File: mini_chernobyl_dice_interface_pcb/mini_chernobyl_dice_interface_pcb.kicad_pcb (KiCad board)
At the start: 2 copper layers, 148 x 49 mm, 23 parts, among them SW1 SW_Push, SW2 ROTARY-ENCODER, U1 CC56-12EWA, U2 CC56-12EWA

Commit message: finish routing
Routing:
- net Net-(H2-Pad8): track 0.00 -> 137.2 mm
- net Net-(H2-Pad7): track 0.00 -> 130.5 mm, vias 0 -> 1
- net Net-(H1-Pad7): track 0.00 -> 101.6 mm
- net Net-(H3-Pad1): track 0.00 -> 81.0 mm
- net Net-(H2-Pad5): track 0.00 -> 73.2 mm, vias 0 -> 1
- net Net-(H2-Pad4): track 0.00 -> 73.1 mm, vias 0 -> 2
- net Net-(H2-Pad3): track 0.00 -> 72.4 mm, vias 0 -> 3
- net Net-(H2-Pad2): track 0.00 -> 70.8 mm, vias 0 -> 1
- net Net-(H3-Pad3): track 0.00 -> 63.0 mm
- net Net-(H3-Pad2): track 0.00 -> 63.0 mm
- net Net-(H2-Pad1): track 0.00 -> 62.8 mm, vias 0 -> 3
- net Net-(H3-Pad4): track 0.00 -> 57.9 mm
- net Net-(H2-Pad6): track 0.00 -> 57.4 mm, vias 0 -> 2
- net Net-(H3-Pad5): track 0.00 -> 54.9 mm
- net Net-(D1-Pad1): track 0.00 -> 47.1 mm, vias 0 -> 1
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- added copper zone on F.Cu, net GND

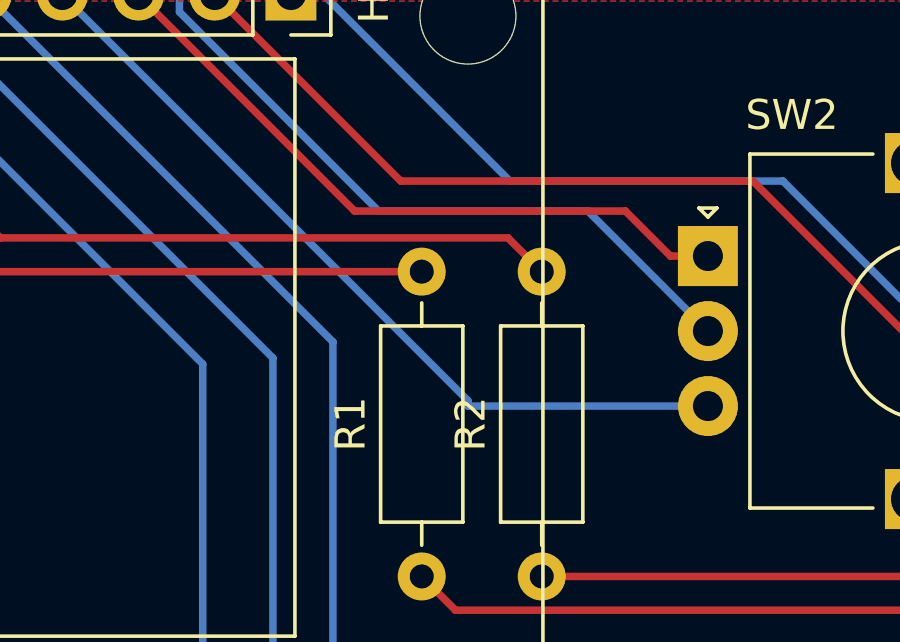
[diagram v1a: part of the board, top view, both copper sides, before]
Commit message: add and clean up labels on pcbs
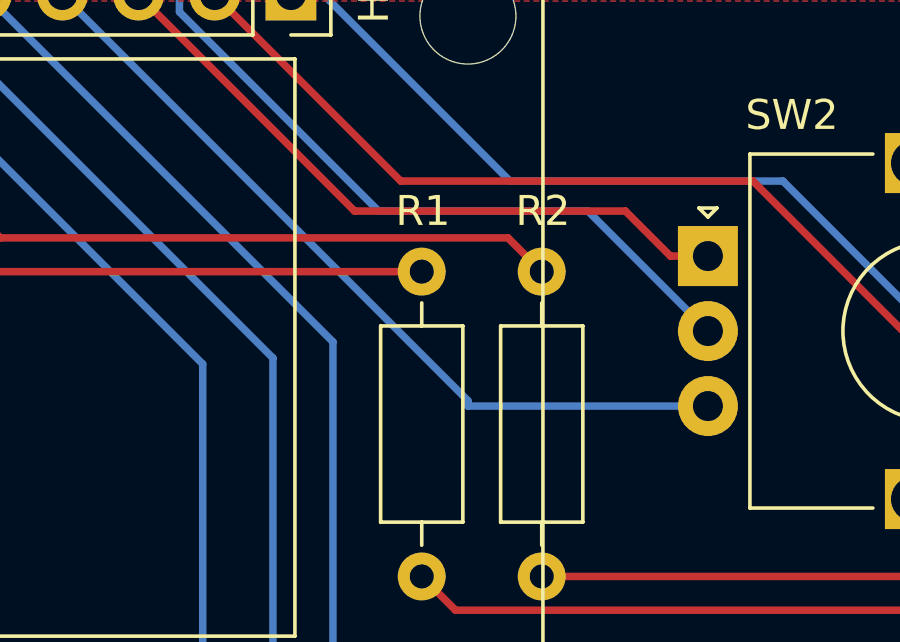
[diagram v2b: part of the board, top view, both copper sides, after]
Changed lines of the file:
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@@
     (46 B.CrtYd user)
     (47 F.CrtYd user)
-    (48 B.Fab user)
+    (48 B.Fab user hide)
     (49 F.Fab user hide)
   )
@@
     (solder_mask_min_width 0.25)
     (aux_axis_origin 0 0)
-    (visible_elements FFFFFF7F)
+    (visible_elements FFFFF77F)
     (pcbplotparams
       (layerselection 0x010fc_ffffffff)
@@
     (descr "Resistor, Axial_DIN0207 series, Axial, Horizontal, pin pitch=10.16mm, 0.25W = 1/4W, length*diameter=6.3*2.5mm^2, http://cdn-reichelt.de/documents/datenblatt/B400/1_4W%23YAG.pdf")
     (tags "Resistor Axial_DIN0207 series Axial Horizontal pin pitch 10.16mm 0.25W = 1/4W length 6.3mm diameter 2.5mm")
-    (fp_text reference R1 (at 5.08 -2.37 90) (layer F.SilkS)
+    (fp_text reference R1 (at 12.18 0.04 180) (layer F.SilkS)
       (effects (font (size 1 1) (thickness 0.15)))
     )
@@
     (descr "Resistor, Axial_DIN0207 series, Axial, Horizontal, pin pitch=10.16mm, 0.25W = 1/4W, length*diameter=6.3*2.5mm^2, http://cdn-reichelt.de/documents/datenblatt/B400/1_4W%23YAG.pdf")
     (tags "Resistor Axial_DIN0207 series Axial Horizontal pin pitch 10.16mm 0.25W = 1/4W length 6.3mm diameter 2.5mm")
-    (fp_text reference R2 (at 5.08 -2.37 90) (layer F.SilkS)
+    (fp_text reference R2 (at 12.18 0.04 180) (layer F.SilkS)
       (effects (font (size 1 1) (thickness 0.15)))
     )
@@
     (descr "Resistor, Axial_DIN0207 series, Axial, Horizontal, pin pitch=10.16mm, 0.25W = 1/4W, length*diameter=6.3*2.5mm^2, http://cdn-reichelt.de/documents/datenblatt/B400/1_4W%23YAG.pdf")
     (tags "Resistor Axial_DIN0207 series Axial Horizontal pin pitch 10.16mm 0.25W = 1/4W length 6.3mm diameter 2.5mm")
-    (fp_text reference R3 (at 5.08 2.37) (layer B.SilkS)
+    (fp_text reference R3 (at 5.08 -2.4) (layer B.SilkS)
       (effects (font (size 1 1) (thickness 0.15)) (justify mirror))
     )
@@
     (descr "Resistor, Axial_DIN0207 series, Axial, Horizontal, pin pitch=10.16mm, 0.25W = 1/4W, length*diameter=6.3*2.5mm^2, http://cdn-reichelt.de/documents/datenblatt/B400/1_4W%23YAG.pdf")
     (tags "Resistor Axial_DIN0207 series Axial Horizontal pin pitch 10.16mm 0.25W = 1/4W length 6.3mm diameter 2.5mm")
-    (fp_text reference R4 (at 5.08 2.37) (layer B.SilkS)
+    (fp_text reference R4 (at 5.08 -2.4) (layer B.SilkS)
       (effects (font (size 1 1) (thickness 0.15)) (justify mirror))
     )
@@
     (descr "Resistor, Axial_DIN0207 series, Axial, Horizontal, pin pitch=10.16mm, 0.25W = 1/4W, length*diameter=6.3*2.5mm^2, http://cdn-reichelt.de/documents/datenblatt/B400/1_4W%23YAG.pdf")
     (tags "Resistor Axial_DIN0207 series Axial Horizontal pin pitch 10.16mm 0.25W = 1/4W length 6.3mm diameter 2.5mm")
-    (fp_text reference R5 (at 5.08 2.37) (layer B.SilkS)
-      (effects (font (size 1 1) (thickness 0.15)) (justify mirror))
-    )
+    (fp_text reference R5 (at 5.08 -2.4) (layer B.SilkS)
+      (effects (font (size 1 1) (thickness 0.15)) (justify mirror))
+    )

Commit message: sync project; add firmware
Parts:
- added D5: LED_ALT, LED_THT:LED_D3.0mm_Horizontal_O1.27mm_Z2.0mm, B.Cu at (90.9, 107.9)
- added D6: LED_ALT, LED_THT:LED_D3.0mm_Horizontal_O1.27mm_Z2.0mm, B.Cu at (74.0, 108.0)
- added D7: LED_ALT, LED_THT:LED_D3.0mm_Horizontal_O1.27mm_Z2.0mm, B.Cu at (57.0, 108.0)
- added R6: R_Small, Resistor_THT:R_Axial_DIN0207_L6.3mm_D2.5mm_P10.16mm_Horizontal, B.Cu at (94.0, 108.0)
- added R7: R_Small, Resistor_THT:R_Axial_DIN0207_L6.3mm_D2.5mm_P10.16mm_Horizontal, B.Cu at (77.0, 108.0)
- added R8: R_Small, Resistor_THT:R_Axial_DIN0207_L6.3mm_D2.5mm_P10.16mm_Horizontal, B.Cu at (60.0, 108.0)
- D2, D3, D4: footprint LED_THT:LED_D3.0mm -> LED_THT:LED_D3.0mm_Horizontal_O1.27mm_Z2.0mm
- H1: footprint Connector_PinSocket_2.54mm:PinSocket_1x10_P2.54mm_Vertical -> mini_chernobyl_dice_interface_pcb:10-PIN-CONNECTOR
- H2, H3: footprint Connector_PinSocket_2.54mm:PinSocket_1x08_P2.54mm_Vertical -> mini_chernobyl_dice_interface_pcb:8-PIN-CONNECTOR
- moved D4 34.1 mm to (107.9, 107.9), turned to 225 degrees
- moved R5 32.1 mm to (111.0, 108.0)
- moved D3 17.3 mm to (124.6, 108.0), turned to 225 degrees
- moved R4 15.4 mm to (128.0, 108.0)
- moved D2 4.20 mm to (141.6, 107.8), turned to 225 degrees
- moved R3 2.42 mm to (145.0, 108.0)
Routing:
- net Net-(H2-Pad8): track 137.2 -> 85.0 mm, vias 0 -> 1
- net Net-(H2-Pad7): track 130.5 -> 85.8 mm
- net Net-(H1-Pad7): track 101.6 -> 136.7 mm
- net Net-(H3-Pad5): track 54.9 -> 34.0 mm, vias 0 -> 1
- net GND: track 43.1 -> 53.6 mm
- net Net-(D5-Pad2): track 0.00 -> 5.60 mm
- net Net-(D6-Pad2): track 0.00 -> 5.54 mm
- net Net-(D7-Pad2): track 0.00 -> 5.54 mm
- net Net-(D3-Pad2): track 3.33 -> 5.94 mm
- net Net-(D2-Pad2): track 3.33 -> 5.86 mm
- net Net-(D4-Pad2): track 3.33 -> 5.60 mm
- net Net-(H3-Pad2): track 63.0 -> 64.2 mm, vias 0 -> 1
- net Net-(H2-Pad6): track 57.4 -> 58.5 mm
